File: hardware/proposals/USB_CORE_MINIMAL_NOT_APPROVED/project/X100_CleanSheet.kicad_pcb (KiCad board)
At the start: 4 copper layers, 45 x 45 mm, 240 parts, among them J401 124019772112A, J501 1040310811, J601 SM04B-GHS-TB(LF)(SN), J701 SM06B-GHS-TB(LF)(SN), J702 SM06B-GHS-TB(LF)(SN), J703 SM06B-GHS-TB(LF)(SN), J704 SM04B-GHS-TB(LF)(SN), J801 OUT1 /GND, J802 OUT2 /GND, J803 OUT3 /GND, J804 OUT4 /GND, J805 OUT5 /GND, J806 OUT6 /GND, J807 SWD:1REF2GND3IO4CLK5NRST, J808 BATTERY/bench3S-6S ONLY, J809 CURRENT monitor only, Q101 DMP6023LSS-13, Q102 BSS138LT1G CAN shutdown, U101 TPS54360BDDAR, U102 AP63203WU-7, U103 TPS7A2033PDBVR, U104 TPS2553DBVR, U105 TPS2116DRLR, U106 TPS2553DBVR, U107 TPS22918DBVR core controlled 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, U108 TPS22918DBVR, U109 SN74CB3Q3245PWR, U110 TLV6700DDCR, U111 SN74LVC1G00DBVR, U112 TMUX1219DBVR ILIM selector, U114 SN74AUP1G32DBVR core sensor EN, U201 STM32H743VIT6, U301 BMI088, U302 SPL06-001, U401 TPD2E2U06QDBZRQ1, U402 SN74LVC1G17DBVR, U403 TPD2E2U06QDBZRQ1, U404 TPD2E2U06QDBZRQ1, U601 TCAN3414DR, U801 TMUX1511PWR, Y201 8.000MHz /CL20pF

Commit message: Connect all MCU VDD and GND with partitioned 3V3 plane
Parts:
- R510: moved to B.Cu
- moved R510 34.7 mm to (120.3, 84.1), turned to 0 degrees
- moved R206 12.1 mm to (91.5, 103.5), turned to -90 degrees
- moved C201 0.67 mm to (105.7, 103.4), turned to 180 degrees
- moved R103 0.60 mm to (108.8, 103.5)
- moved TP309 0.46 mm to (110.0, 99.5)
- moved TP205 0.32 mm to (106.3, 104.7)
- moved C203 0.12 mm to (91.6, 90.5)
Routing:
- net 3V3_MCU: track 206.5 -> 279.2 mm, vias 14 -> 20
- net GND: track 116.8 -> 121.6 mm, vias 42 -> 43
- net VCAP1: track 6.95 -> 5.12 mm
- added copper zone on In2.Cu, net 3V3_MCU

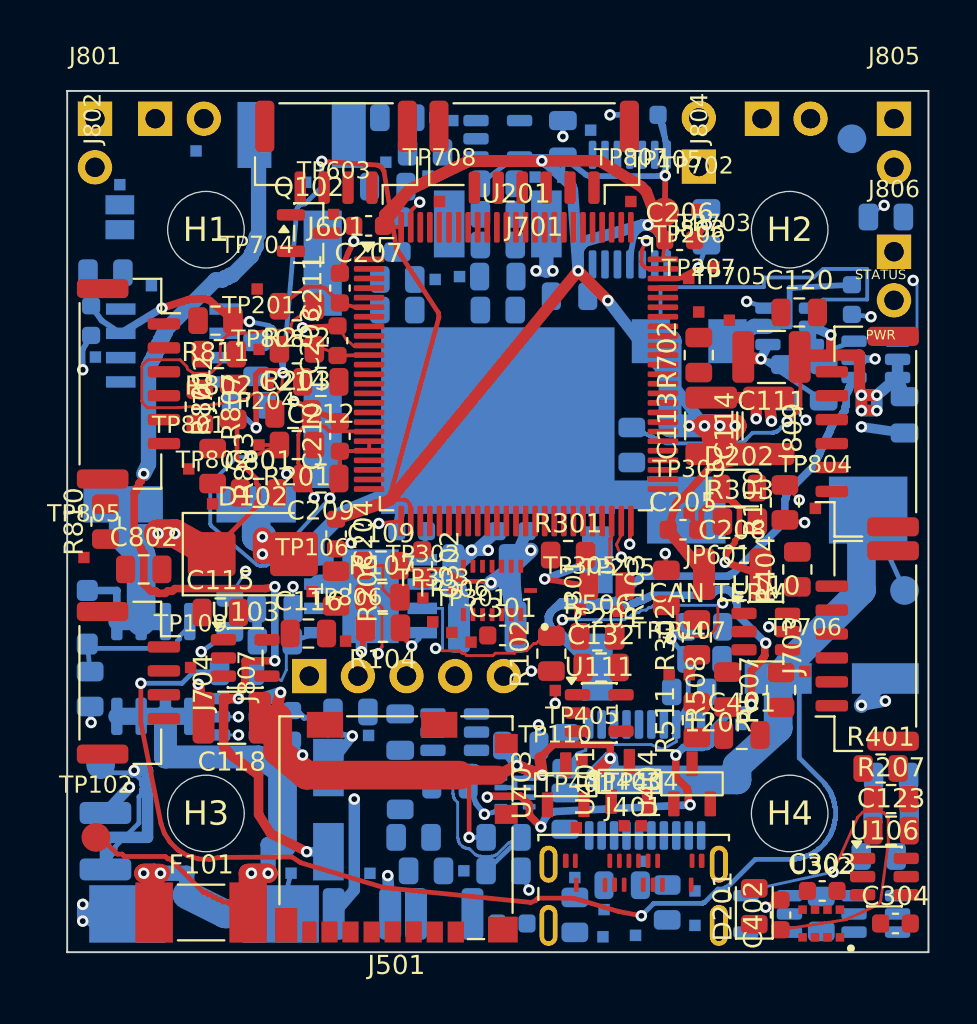
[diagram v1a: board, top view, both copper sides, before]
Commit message: Route HSE and USB and extend switched SD power
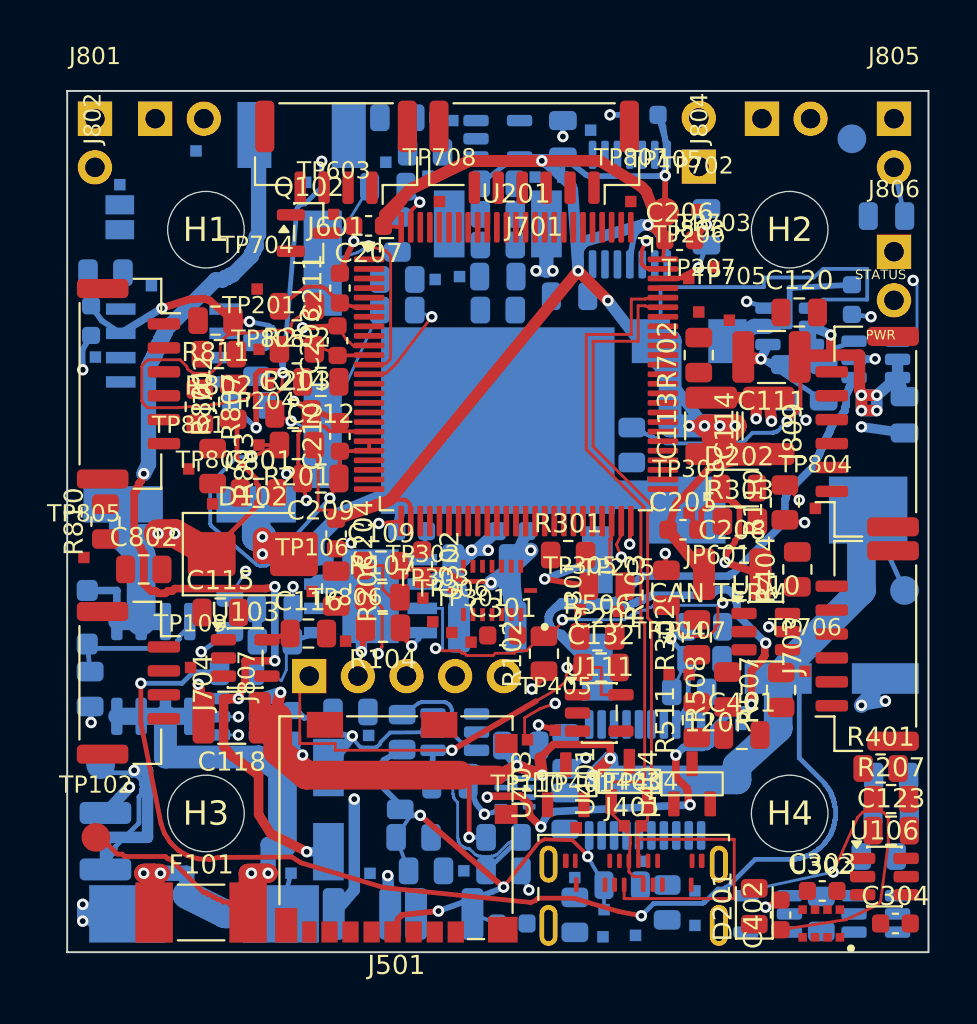
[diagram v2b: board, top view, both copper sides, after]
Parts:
- moved C134 37.0 mm to (120.3, 84.0), turned to 0 degrees
- moved R510 26.9 mm to (110.0, 108.9)
- moved R501 15.1 mm to (95.0, 111.0), turned to -90 degrees
- moved TP110 2.96 mm to (101.5, 111.4)
- moved TP405 2.09 mm to (103.0, 110.9)
- moved R102 0.39 mm to (102.4, 106.9)
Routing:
- net USB_DM: track 0.00 -> 50.2 mm
- net USB_DP: track 0.00 -> 38.8 mm
- net 3V3_SD: track 0.00 -> 32.2 mm, vias 0 -> 4
- net HSE_IN: track 0.00 -> 15.2 mm, vias 0 -> 1
- net GND: track 121.6 -> 132.2 mm
- net HSE_XOUT: track 0.00 -> 9.94 mm, vias 0 -> 1
- net 3V3_SD_SWITCHED_SRC: track 0.00 -> 5.81 mm
- net HSE_OUT: track 0.00 -> 5.64 mm, vias 0 -> 1
- net EXT_FAULT: track 37.3 -> 39.0 mm
- net 3V3_MCU: track 279.2 -> 280.8 mm, vias 20 -> 22
- net 3V3_SENSOR: track 0.00 -> 1.26 mm
